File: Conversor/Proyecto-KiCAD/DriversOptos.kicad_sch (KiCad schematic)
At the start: 29 parts, among them U10 ACPL-P480, U11 ACPL-P480, U12 2ED21834-S06J, U13 2ED21834-S06J, U8 ACPL-P480, U9 ACPL-P480

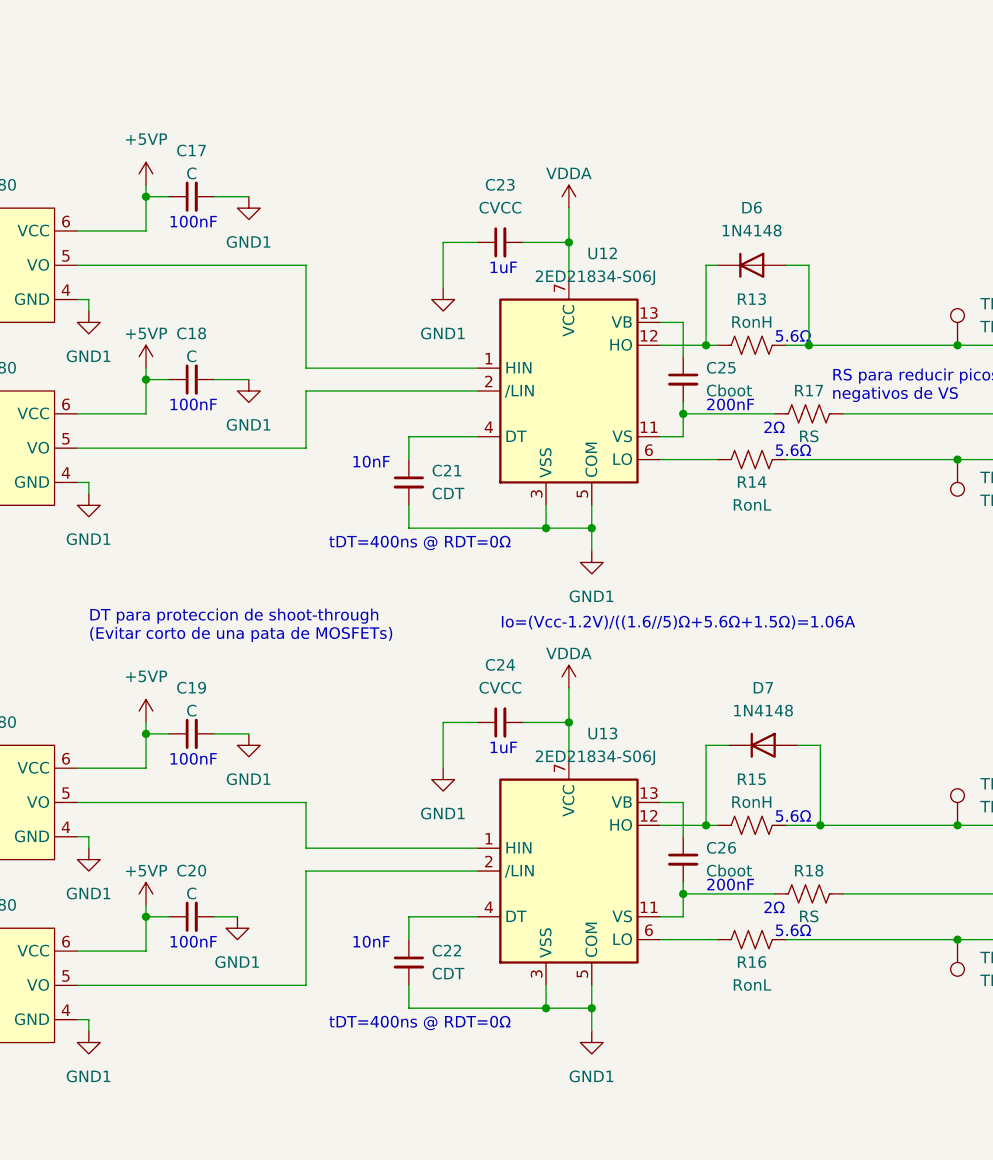
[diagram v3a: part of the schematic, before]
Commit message: Agregar resistencias de pull-up faltantes
- Agregar resistencias de pull-up a la salida de cada inversor del
74LS06
- Crear plano de U5V en la capa superior alrededor del FTDI
- Ponerle los valores a los componentes para poder generar correctamente
el BOM (Bill of Materials)
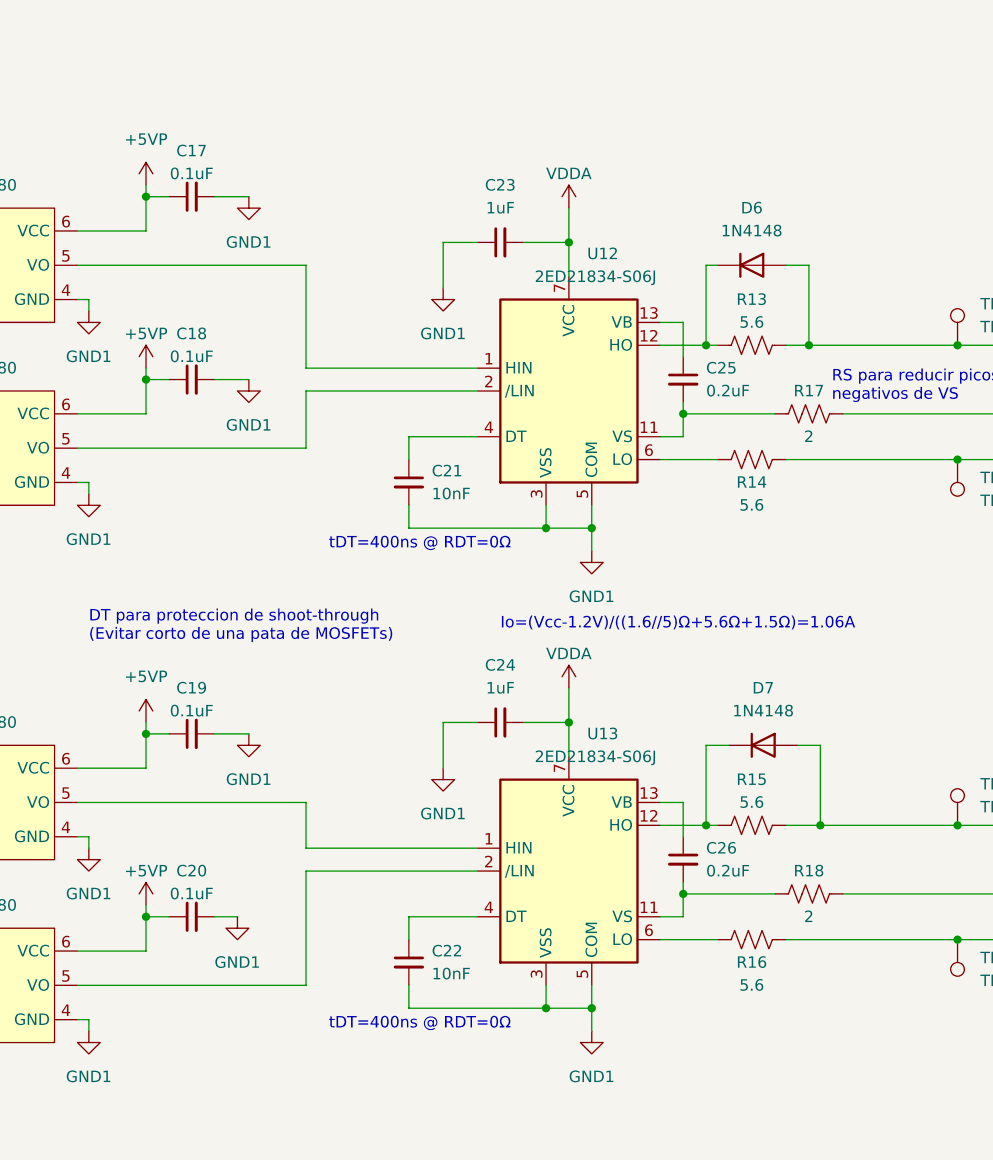
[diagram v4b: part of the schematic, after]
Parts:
- C17, C18, C19, C20: value C -> 0.1uF
- C21, C22: value CDT -> 10nF
- C23, C24: value CVCC -> 1uF
- C25, C26: value Cboot -> 0.2uF
- R13, R15: value RonH -> 5.6
- R14, R16: value RonL -> 5.6
- R17, R18: value RS -> 2
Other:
- note removed: "100nF"
- note removed: "10nF"
- note removed: "1uF"
- note removed: "200nF"
- note removed: "2Ω"
- note removed: "5.6Ω"
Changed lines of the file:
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@@
-    (effects (font (size 1.27 1.27)) (justify left bottom))
-  )
-  (text "2Ω" (at 213.36 127 0)
-    (effects (font (size 1.27 1.27)) (justify left bottom))
-  )
-  (text "100nF" (at 147.32 50.8 0)
-    (effects (font (size 1.27 1.27)) (justify left bottom))
-  )
-  (text "200nF" (at 207.01 124.46 0)
-    (effects (font (size 1.27 1.27)) (justify left bottom))
-  )
-  (text "5.6Ω" (at 214.63 63.5 0)
-    (effects (font (size 1.27 1.27)) (justify left bottom))
-  )
-  (text "100nF" (at 147.32 110.49 0)
-    (effects (font (size 1.27 1.27)) (justify left bottom))
-  )
-  (text "2Ω" (at 213.36 73.66 0)
-    (effects (font (size 1.27 1.27)) (justify left bottom))
-  )
-  (text "5.6Ω" (at 214.63 76.2 0)
-    (effects (font (size 1.27 1.27)) (justify left bottom))
-  )
-  (text "5.6Ω" (at 214.63 116.84 0)
     (effects (font (size 1.27 1.27)) (justify left bottom))
   )
   (text "RS para reducir picos\nnegativos de VS" (at 220.98 69.85 0)
-    (effects (font (size 1.27 1.27)) (justify left bottom))
-  )
-  (text "1uF" (at 182.88 55.88 0)
-    (effects (font (size 1.27 1.27)) (justify left bottom))
-  )
-  (text "5.6Ω" (at 214.63 129.54 0)
     (effects (font (size 1.27 1.27)) (justify left bottom))
   )
@@
     (effects (font (size 1.27 1.27)) (justify left bottom))
   )
-  (text "200nF" (at 207.01 71.12 0)
-    (effects (font (size 1.27 1.27)) (justify left bottom))
-  )
   (text "tDT=400ns @ RDT=0Ω" (at 165.1 139.7 0)
-    (effects (font (size 1.27 1.27)) (justify left bottom))
-  )
-  (text "100nF" (at 147.32 71.12 0)
     (effects (font (size 1.27 1.27)) (justify left bottom))
   )
@@
     (effects (font (size 2.54 2.54) (thickness 0.508) bold) (justify left bottom))
   )
-  (text "1uF" (at 182.88 109.22 0)
-    (effects (font (size 1.27 1.27)) (justify left bottom))
-  )
   (text "tDT=400ns @ RDT=0Ω" (at 165.1 86.36 0)
-    (effects (font (size 1.27 1.27)) (justify left bottom))
-  )
-  (text "100nF" (at 147.32 130.81 0)
-    (effects (font (size 1.27 1.27)) (justify left bottom))
-  )
-  (text "10nF" (at 167.64 77.47 0)
-    (effects (font (size 1.27 1.27)) (justify left bottom))
-  )
-  (text "10nF" (at 167.64 130.81 0)
     (effects (font (size 1.27 1.27)) (justify left bottom))
   )
@@
       (effects (font (size 1.27 1.27)) (justify left))
     )
-    (property "Value" "CDT" (id 1) (at 176.53 133.3562 0)
+    (property "Value" "10nF" (id 1) (at 176.53 133.3562 0)
       (effects (font (size 1.27 1.27)) (justify left))
     )
@@
     (in_bom yes) (on_board yes)
     (property "Reference" "C19" (id 0) (at 149.86 101.6 90))
-    (property "Value" "C" (id 1) (at 149.86 104.14 90))
+    (property "Value" "0.1uF" (id 1) (at 149.86 104.14 90))
     (property "Footprint" "Capacitor_SMD:C_1206_3216Metric_Pad1.33x1.80mm_HandSolder" (id 2) (at 149.86 106.68 0)
       (effects (font (size 1.27 1.27)) hide)
@@
       (effects (font (size 1.27 1.27)) (justify left))
     )
-    (property "Value" "Cboot" (id 1) (at 207.01 121.9262 0)
+    (property "Value" "0.2uF" (id 1) (at 207.01 121.9262 0)
       (effects (font (size 1.27 1.27)) (justify left))
     )
@@
     (in_bom yes) (on_board yes)
     (property "Reference" "C18" (id 0) (at 149.86 62.23 90))
-    (property "Value" "C" (id 1) (at 149.86 64.77 90))
+    (property "Value" "0.1uF" (id 1) (at 149.86 64.77 90))
     (property "Footprint" "Capacitor_SMD:C_1206_3216Metric_Pad1.33x1.80mm_HandSolder" (id 2) (at 149.86 67.31 0)
       (effects (font (size 1.27 1.27)) hide)
@@
     (in_bom yes) (on_board yes)
     (property "Reference" "R15" (id 0) (at 212.09 111.76 90))
-    (property "Value" "RonH" (id 1) (at 212.09 114.3 90))
+    (property "Value" "5.6" (id 1) (at 212.09 114.3 90))
     (property "Footprint" "Resistor_SMD:R_1206_3216Metric_Pad1.30x1.75mm_HandSolder" (id 2) (at 212.344 115.824 90)
       (effects (font (size 1.27 1.27)) hide)
@@
     (in_bom yes) (on_board yes)
     (property "Reference" "C17" (id 0) (at 149.86 41.91 90))
-    (property "Value" "C" (id 1) (at 149.86 44.45 90))
+    (property "Value" "0.1uF" (id 1) (at 149.86 44.45 90))
     (property "Footprint" "Capacitor_SMD:C_1206_3216Metric_Pad1.33x1.80mm_HandSolder" (id 2) (at 149.86 46.99 0)
       (effects (font (size 1.27 1.27)) hide)
@@
     (in_bom yes) (on_board yes)
     (property "Reference" "R17" (id 0) (at 218.44 68.58 90))
-    (property "Value" "RS" (id 1) (at 218.44 73.66 90))
+    (property "Value" "2" (id 1) (at 218.44 73.66 90))
     (property "Footprint" "Resistor_SMD:R_1206_3216Metric_Pad1.30x1.75mm_HandSolder" (id 2) (at 218.694 70.104 90)
       (effects (font (size 1.27 1.27)) hide)
@@
     (in_bom yes) (on_board yes) (fields_autoplaced)
     (property "Reference" "C23" (id 0) (at 184.1563 45.72 90))
-    (property "Value" "CVCC" (id 1) (at 184.1563 48.26 90))
+    (property "Value" "1uF" (id 1) (at 184.1563 48.26 90))
     (property "Footprint" "Capacitor_SMD:C_1206_3216Metric_Pad1.33x1.80mm_HandSolder" (id 2) (at 184.15 52.07 0)
       (effects (font (size 1.27 1.27)) hide)
@@
     (in_bom yes) (on_board yes)
     (property "Reference" "R14" (id 0) (at 212.09 78.74 90))
-    (property "Value" "RonL" (id 1) (at 212.09 81.28 90))
+    (property "Value" "5.6" (id 1) (at 212.09 81.28 90))
     (property "Footprint" "Resistor_SMD:R_1206_3216Metric_Pad1.30x1.75mm_HandSolder" (id 2) (at 212.344 75.184 90)
       (effects (font (size 1.27 1.27)) hide)
@@
     (in_bom yes) (on_board yes)
     (property "Reference" "R13" (id 0) (at 212.09 58.42 90))
-    (property "Value" "RonH" (id 1) (at 212.09 60.96 90))
+    (property "Value" "5.6" (id 1) (at 212.09 60.96 90))
     (property "Footprint" "Resistor_SMD:R_1206_3216Metric_Pad1.30x1.75mm_HandSolder" (id 2) (at 212.344 62.484 90)
       (effects (font (size 1.27 1.27)) hide)
@@
     (in_bom yes) (on_board yes)
     (property "Reference" "C20" (id 0) (at 149.86 121.92 90))
-    (property "Value" "C" (id 1) (at 149.86 124.46 90))
+    (property "Value" "0.1uF" (id 1) (at 149.86 124.46 90))
     (property "Footprint" "Capacitor_SMD:C_1206_3216Metric_Pad1.33x1.80mm_HandSolder" (id 2) (at 149.86 127 0)
       (effects (font (size 1.27 1.27)) hide)
@@
       (effects (font (size 1.27 1.27)) (justify left))
     )
-    (property "Value" "CDT" (id 1) (at 176.53 80.0162 0)
+    (property "Value" "10nF" (id 1) (at 176.53 80.0162 0)
       (effects (font (size 1.27 1.27)) (justify left))
     )
@@
       (effects (font (size 1.27 1.27)) (justify left))
     )
-    (property "Value" "Cboot" (id 1) (at 207.01 68.58 0)
+    (property "Value" "0.2uF" (id 1) (at 207.01 68.58 0)
       (effects (font (size 1.27 1.27)) (justify left))
     )
@@
     (in_bom yes) (on_board yes)
     (property "Reference" "R18" (id 0) (at 218.44 121.92 90))
-    (property "Value" "RS" (id 1) (at 218.44 127 90))
+    (property "Value" "2" (id 1) (at 218.44 127 90))
     (property "Footprint" "Resistor_SMD:R_1206_3216Metric_Pad1.30x1.75mm_HandSolder" (id 2) (at 218.694 123.444 90)
       (effects (font (size 1.27 1.27)) hide)
@@
     (in_bom yes) (on_board yes) (fields_autoplaced)
     (property "Reference" "C24" (id 0) (at 184.1563 99.06 90))
-    (property "Value" "CVCC" (id 1) (at 184.1563 101.6 90))
+    (property "Value" "1uF" (id 1) (at 184.1563 101.6 90))
     (property "Footprint" "Capacitor_SMD:C_1206_3216Metric_Pad1.33x1.80mm_HandSolder" (id 2) (at 184.15 105.41 0)
       (effects (font (size 1.27 1.27)) hide)
@@
     (in_bom yes) (on_board yes)
     (property "Reference" "R16" (id 0) (at 212.09 132.08 90))
-    (property "Value" "RonL" (id 1) (at 212.09 134.62 90))
+    (property "Value" "5.6" (id 1) (at 212.09 134.62 90))
     (property "Footprint" "Resistor_SMD:R_1206_3216Metric_Pad1.30x1.75mm_HandSolder" (id 2) (at 212.344 128.524 90)
       (effects (font (size 1.27 1.27)) hide)

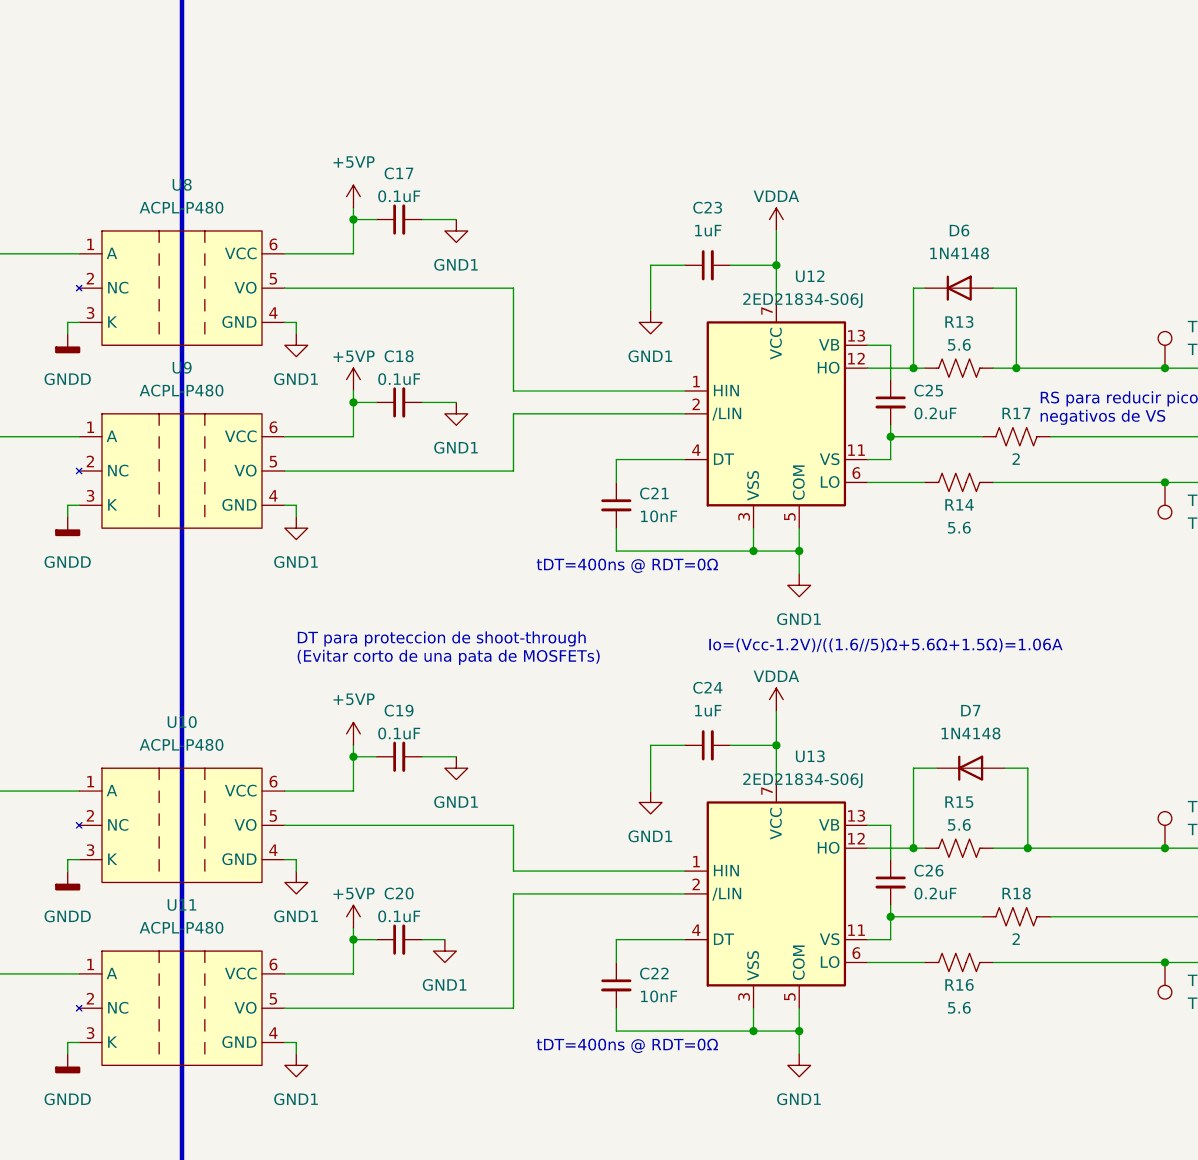
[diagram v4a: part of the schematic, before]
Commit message: Eliminar resistencias de pull-up de SCL y SDAI
- Se pueden remover las Rpu del lado del sensor ya que las Rpu de esas
lineas estan del otro lado (la barrera de aislación proteje de daños).
La de SDAO tiene que quedar por la salida open-drain del LM5056.
- También cambiar las Rpu de 10k a 4k7, porque la capacidad del bus es
muy baja (un solo esclavo y pistas cortas). Así se disminuye es rise
time (Rpu*Cbus) a la mitad.
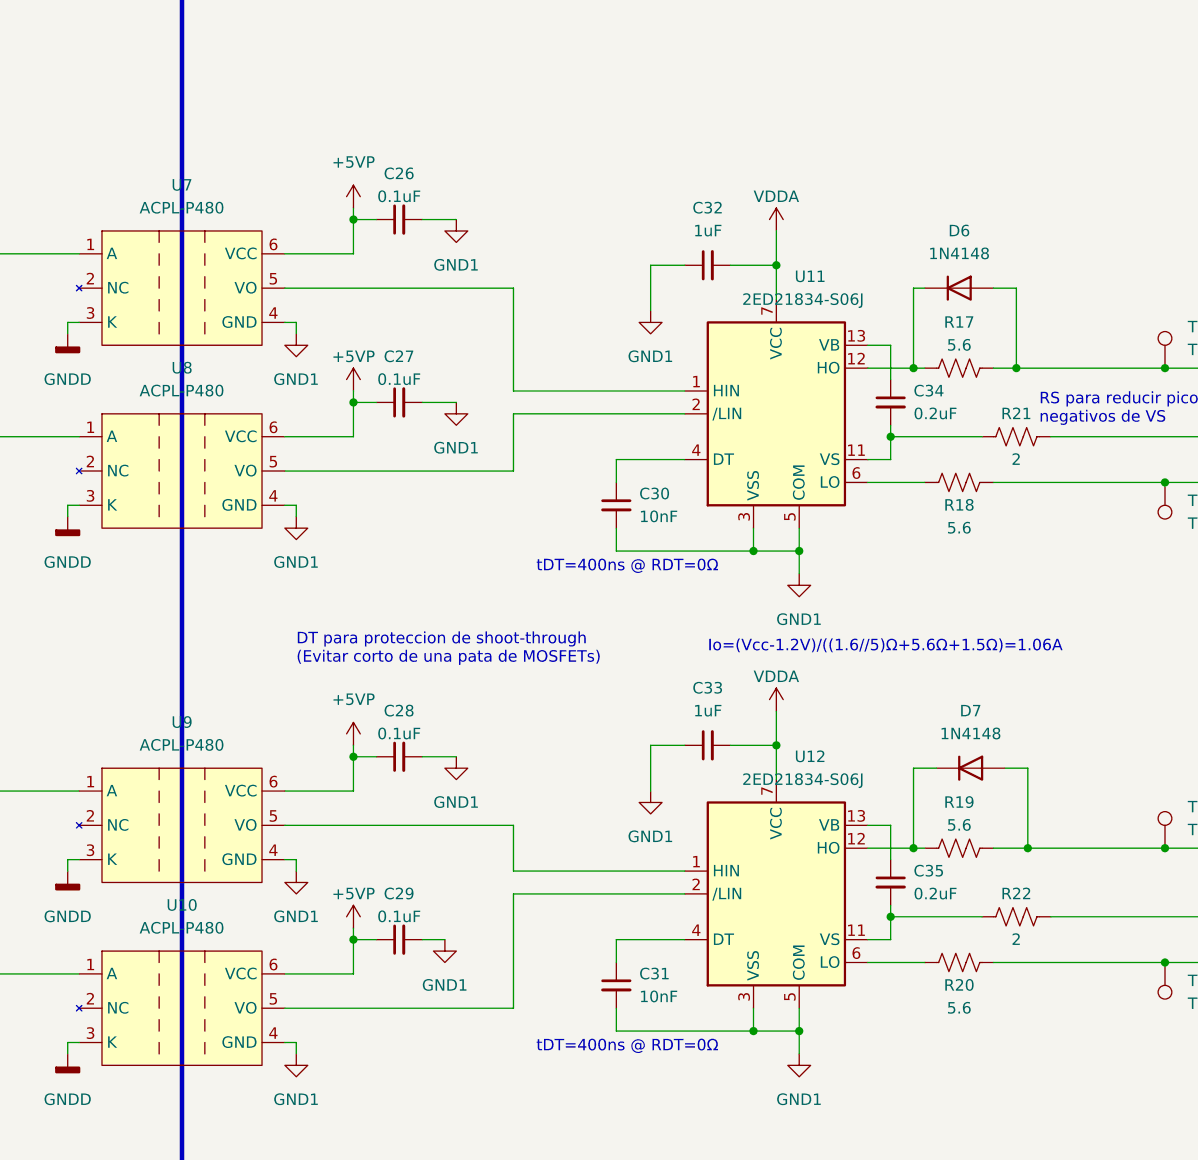
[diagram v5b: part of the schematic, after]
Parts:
- renumbered C17 to C26, C18 to C27, C19 to C28, C20 to C29, C21 to C30, C22 to C31, C23 to C32, C24 to C33, C25 to C34, C26 to C35, R13 to R17, R14 to R18, R15 to R19, R16 to R20, R17 to R21, R18 to R22, U11 to U10, U12 to U11, U13 to U12, U8 to U7, U9 to U8, U10 to U9
